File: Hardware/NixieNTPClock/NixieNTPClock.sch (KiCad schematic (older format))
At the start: 20 parts

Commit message: Add documentation with siemens datasheet Add farnel refs and component refs in schematic
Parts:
- removed Q?: BC547, Package_TO_SOT_THT:TO-92_Inline, symbol Transistor_BJT:BC547
- added Q?: BC850, Package_TO_SOT_SMD:SOT-23, symbol Transistor_BJT:BC850
- D?: value D_Shockley -> MBRS3200T3G; Farnel (none) -> 1838812
- Q?: footprint (none) -> TO_SOT_Packages_SMD:TO-252-2; Farnel (none) -> 2453852
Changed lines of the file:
@@
 EESchema Schematic File Version 4
+LIBS:NixieNTPClock-cache
 EELAYER 30 0
 EELAYER END
@@
 U 1 1 5DB6317C
 P 3750 6800
-F 0 "C?" H 3865 6846 50  0000 L CNN
+F 0 "C?" H 3800 6900 50  0000 L CNN
 F 1 "100nF" H 3800 6700 50  0000 L CNN
 F 2 "" H 3788 6650 50  0001 C CNN
@@
 	1    0    0    -1
 $EndComp
-$Comp
-L Transistor_BJT:BC547 Q?
-U 1 1 5DB638E9
-P 4200 6800
-F 0 "Q?" H 4100 6950 50  0000 L CNN
-F 1 "BC547" H 3950 6650 50  0000 L CNN
-F 2 "Package_TO_SOT_THT:TO-92_Inline" H 4400 6725 50  0001 L CIN
-F 3 "http://www.fairchildsemi.com/ds/BC/BC547.pdf" H 4200 6800 50  0001 L CNN
-	1    4200 6800
-	-1   0    0    -1
-$EndComp
 Wire Wire Line
 	3650 6450 3750 6450
-Wire Wire Line
-	4100 6450 4100 6600
 Wire Wire Line
 	3750 6450 3750 6650
@@
 Wire Wire Line
 	4100 6150 4100 6450
-Connection ~ 4100 6450
 Wire Wire Line
 	3150 5450 3150 5950
@@
 F 0 "Q?" H 4950 6350 50  0000 L CNN
 F 1 "Q_NMOS_GDS" H 5200 6300 50  0000 L CNN
-F 2 "" H 5300 6650 50  0001 C CNN
+F 2 "TO_SOT_Packages_SMD:TO-252-2" H 5300 6650 50  0001 C CNN
 F 3 "~" H 5100 6550 50  0001 C CNN
+F 4 "2453852" H 5100 6550 50  0001 C CNN "Farnel"
 	1    5100 6550
 	1    0    0    -1
@@
 P 5550 6200
 F 0 "D?" H 5550 5984 50  0000 C CNN
-F 1 "D_Shockley" H 5550 6075 50  0000 C CNN
+F 1 "MBRS3200T3G" H 5550 6075 50  0000 C CNN
 F 2 "" H 5550 6200 50  0001 C CNN
 F 3 "~" H 5550 6200 50  0001 C CNN
+F 4 "1838812" H 5550 6200 50  0001 C CNN "Farnel"
 	1    5550 6200
 	-1   0    0    1
@@
 	6500 6200 6250 6200
 Connection ~ 6250 6200
+$Comp
+L Transistor_BJT:BC850 Q?
+U 1 1 5DB5C42D
+P 4200 6800
+F 0 "Q?" H 4050 6900 50  0000 L CNN
+F 1 "BC850" H 3950 6650 50  0000 L CNN
+F 2 "Package_TO_SOT_SMD:SOT-23" H 4400 6725 50  0001 L CIN
+F 3 "http://www.infineon.com/dgdl/Infineon-BC847SERIES_BC848SERIES_BC849SERIES_BC850SERIES-DS-v01_01-en.pdf?fileId=db3a304314dca389011541d4630a1657" H 4200 6800 50  0001 L CNN
+F 4 "1081241" H 4200 6800 50  0001 C CNN "Farnel"
+	1    4200 6800
+	-1   0    0    -1
+$EndComp
+Wire Wire Line
+	4100 6600 4100 6450
+Connection ~ 4100 6450
 $EndSCHEMATC

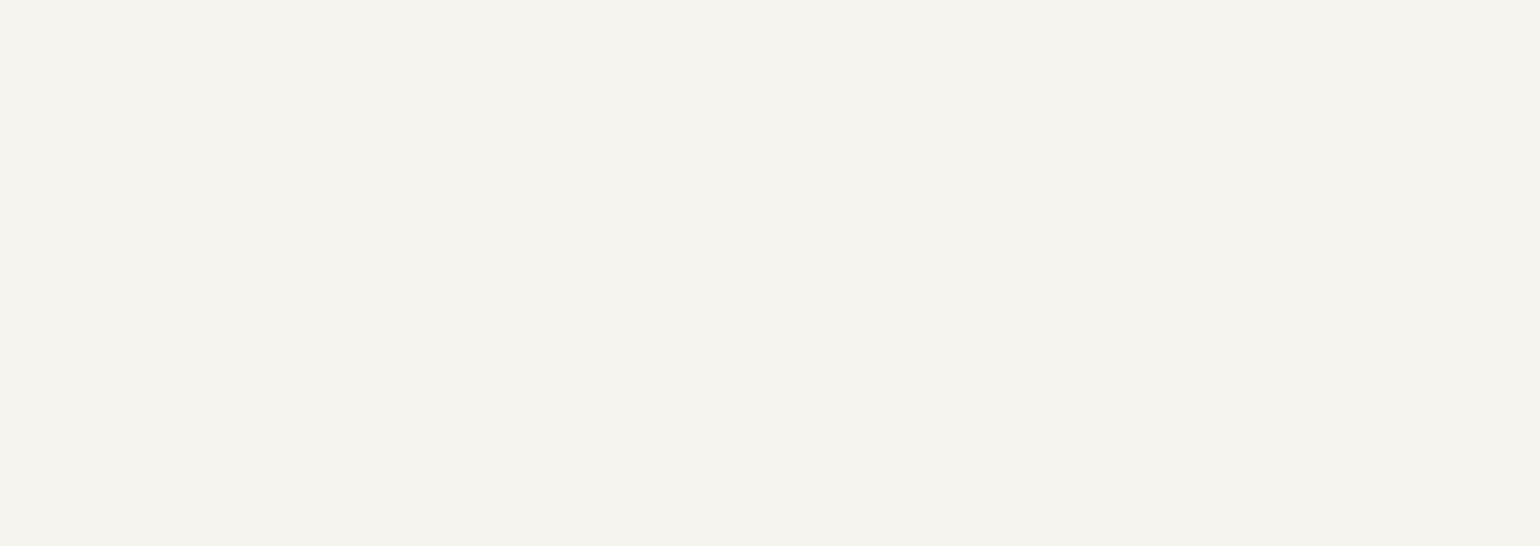
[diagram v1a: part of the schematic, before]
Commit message: Add nixie command in schema, nixie library in project and pdf in documentation
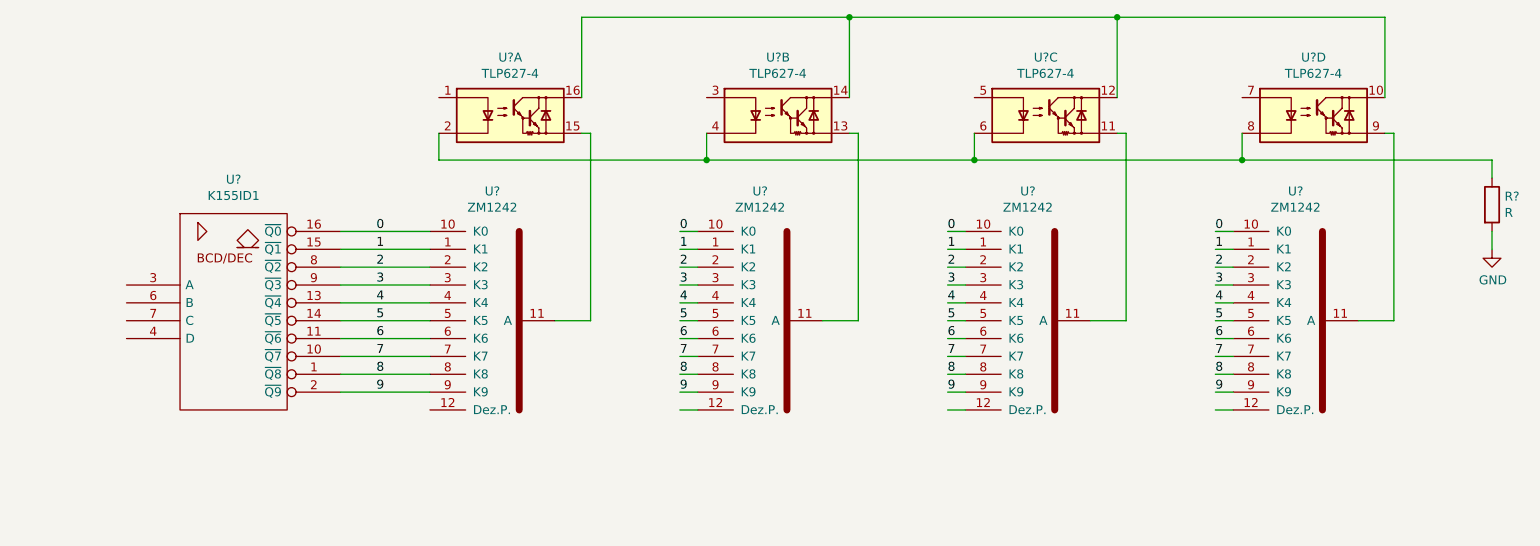
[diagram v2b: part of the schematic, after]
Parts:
- added R?: R, symbol Device:R
- added U?: K155ID1, Housings_DIP:DIP-16_W7.62mm_Socket, symbol 74xx_IEEE:74141
- added U? (x4): ZM1242, symbol nixieValve:ZM1242
- added U? (x4): TLP627-4, Package_DIP:DIP-16_W7.62mm, symbol Isolator:TLP627-4
- D?: Farnel 1838812 -> (none); Farnell (none) -> 1838812
- Q?: Farnel 1081241 -> (none); Farnell (none) -> 1081241
- Q?: Farnel 2453852 -> (none); Farnell (none) -> 2453852
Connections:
- net GND: now also R?.2, U?.12 (GND)
- new net: U?.11 (A), U?.15
- new net: U?.11 (A), U?.13
- new net: U?.11, U?.11 (A)
- new net: U?.11 (A), U?.9
- new net: U?.10, U?.12, U?.14, U?.16
- new net: R?.1, U?.2, U?.4, U?.6, U?.8
- new net 0: U?.10 (K0), U?.10 (K0), U?.10 (K0), U?.10 (K0), U?.16 (~Q0)
- new net 1: U?.1 (K1), U?.1 (K1), U?.1 (K1), U?.1 (K1), U?.15 (~Q1)
- new net 2: U?.2 (K2), U?.2 (K2), U?.2 (K2), U?.2 (K2), U?.8 (~Q2)
- new net 3: U?.3 (K3), U?.3 (K3), U?.3 (K3), U?.3 (K3), U?.9 (~Q3)
- new net 4: U?.13 (~Q4), U?.4 (K4), U?.4 (K4), U?.4 (K4), U?.4 (K4)
- new net 5: U?.14 (~Q5), U?.5 (K5), U?.5 (K5), U?.5 (K5), U?.5 (K5)
- new net 6: U?.11 (~Q6), U?.6 (K6), U?.6 (K6), U?.6 (K6), U?.6 (K6)
- new net 7: U?.10 (~Q7), U?.7 (K7), U?.7 (K7), U?.7 (K7), U?.7 (K7)
- new net 8: U?.1 (~Q8), U?.8 (K8), U?.8 (K8), U?.8 (K8), U?.8 (K8)
- new net 9: U?.2 (~Q9), U?.9 (K9), U?.9 (K9), U?.9 (K9), U?.9 (K9)
- new net VCC: U?.5 (VCC)

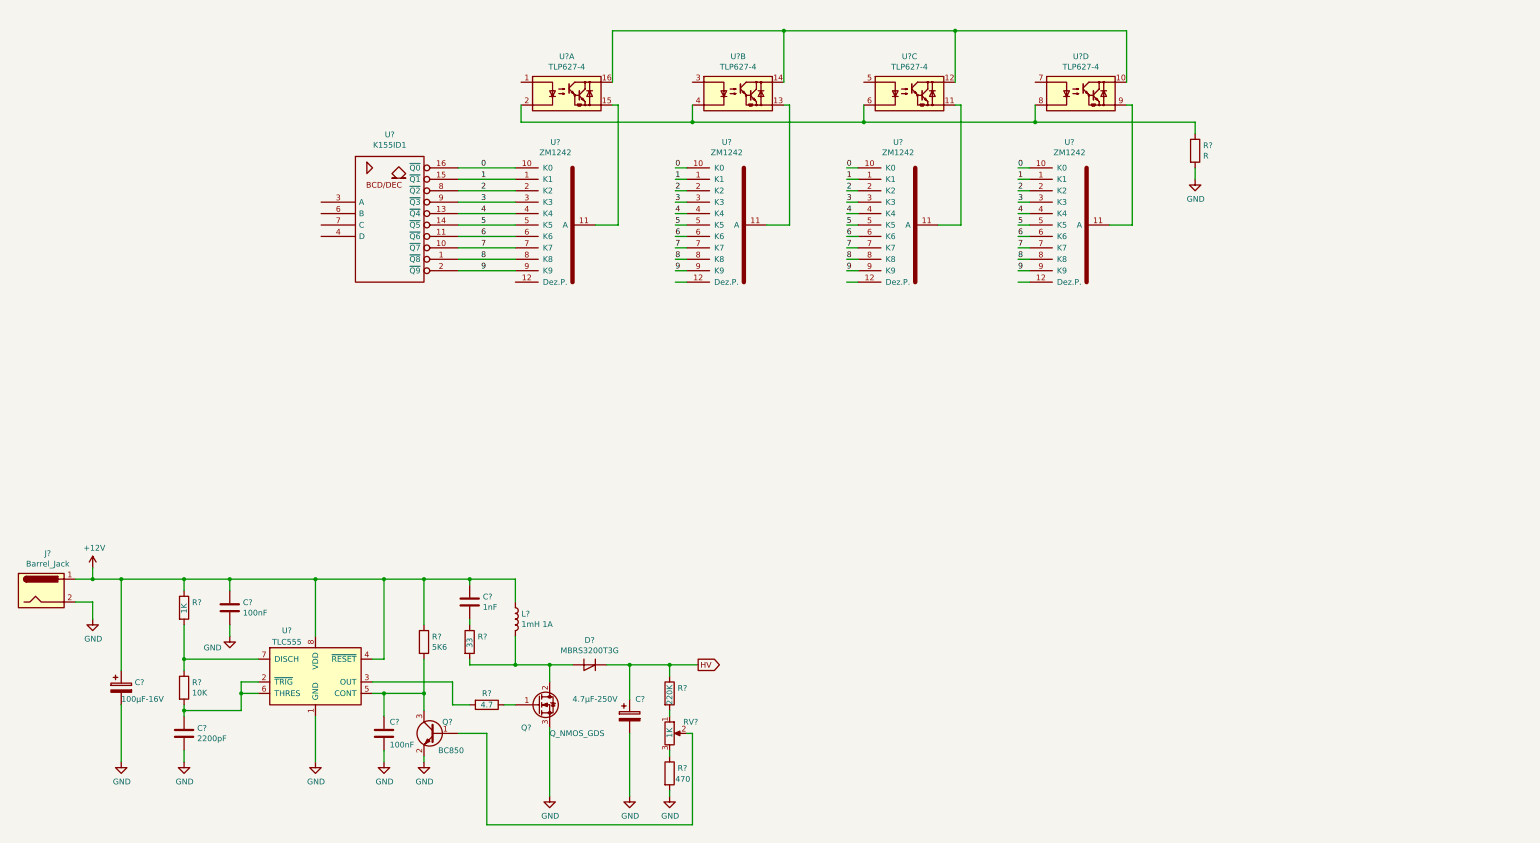
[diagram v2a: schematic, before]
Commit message: nixie command finished, add 5V DC power supply and temp sensor
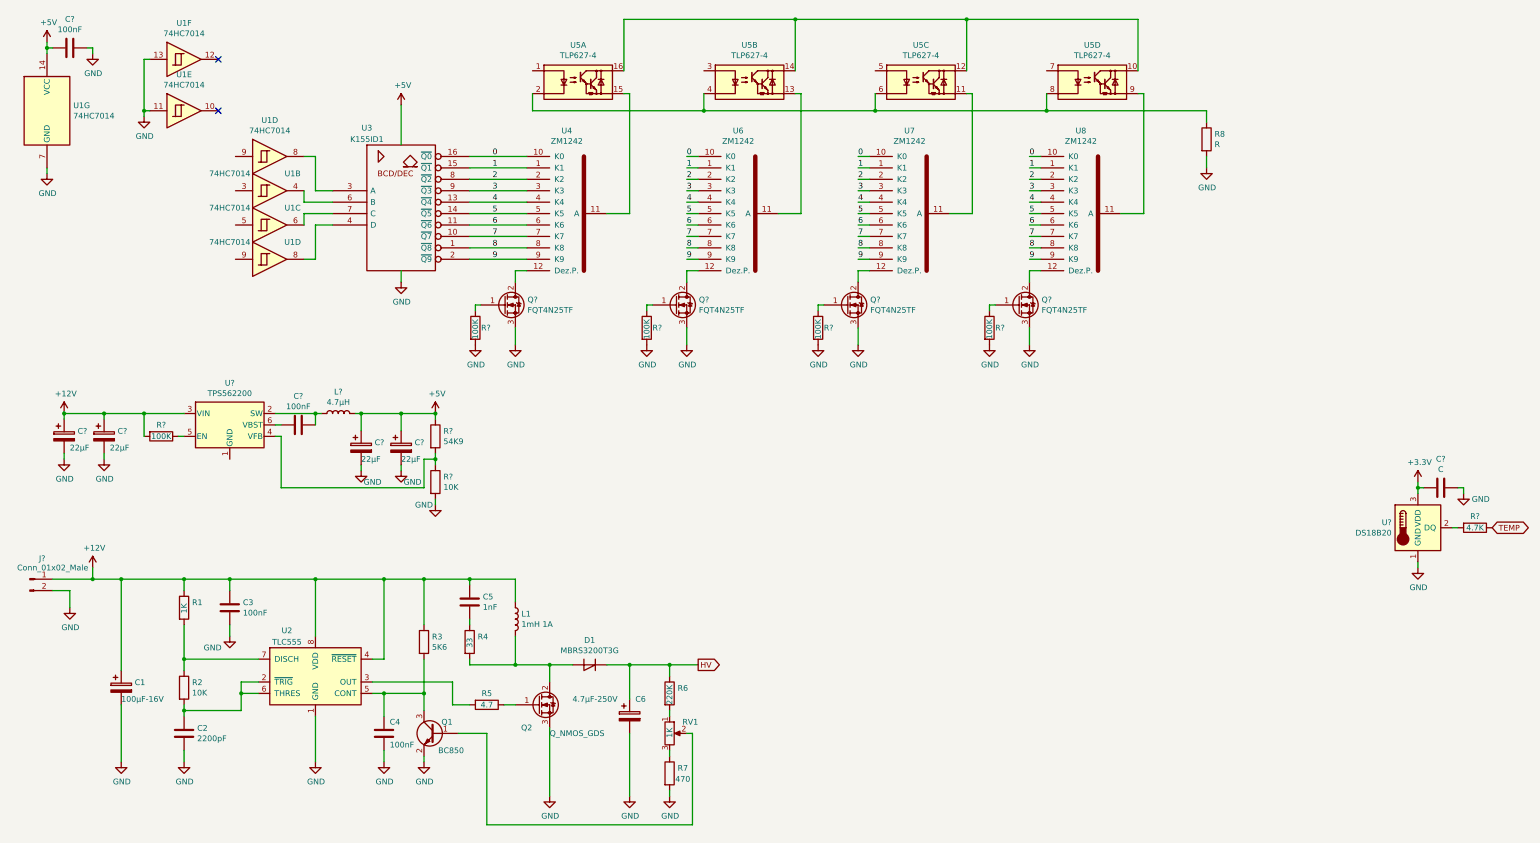
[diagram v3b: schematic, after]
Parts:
- removed J?: Barrel_Jack, symbol Connector:Barrel_Jack
- added C? (x2): 100nF, symbol Device:C
- added C?: C, symbol Device:C
- added C? (x4): 22µF, symbol Device:CP
- added J?: Conn_01x02_Male, symbol Connector:Conn_01x02_Male
- added L?: 4.7µH, symbol Device:L
- added Q? (x4): FQT4N25TF, TO_SOT_Packages_SMD:SOT-223-3_TabPin2, symbol Device:Q_NMOS_GDS
- added R?: 4.7K, symbol Device:R
- added R? (x5): 100K, symbol Device:R
- added R?: 54K9, symbol Device:R
- added R?: 10K, symbol Device:R
- added U1 (x2): 74HC7014, Package_SO:SOIC-14_3.9x8.7mm_P1.27mm, symbol 74xx:74HC7014
- added U?: DS18B20, Package_TO_SOT_THT:TO-92_Inline, symbol Sensor_Temperature:DS18B20
- added U?: TPS562200, Package_TO_SOT_SMD:SOT-23-6, symbol Regulator_Switching:TPS562200
- gave numbers to parts that had none: 26
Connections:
- net +12V: now also C?.1, C?.1, J?.1 (Pin_1), R?.2, U?.3 (VIN)
- net GND: now also C?.1, C?.1, C?.2, C?.2, C?.2, C?.2, J?.2 (Pin_2), Q?.3 (S), Q?.3 (S), Q?.3 (S), Q?.3 (S), R?.2, R?.2, R?.2, R?.2, R?.2, U1.11, U1.13, U1.7 (GND), U?.1 (GND)
- net at U3.3 (A): now also U1.8
- net at U3.4 (D): now also U1.8
- net at U3.6 (B): now also U1.4
- net at U3.7 (C): now also U1.6
- net at U4.12 (Dez.P.): now also Q?.2 (D)
- net at U6.12 (Dez.P.): now also Q?.2 (D)
- net at U7.12 (Dez.P.): now also Q?.2 (D)
- net at U8.12 (Dez.P.): now also Q?.2 (D)
- net VCC renamed +5V
- net +5V: now also C?.1, C?.1, C?.2, L?.2, R?.1, U1.14 (VCC)
- new net: R?.2, U?.2 (DQ)
- new net: Q?.1 (G), R?.1 (x4)
- new net: C?.1, L?.1, U?.2 (SW)
- new net: R?.1, R?.2, U?.4 (VFB)
- new net: R?.1, U?.5 (EN)
- new net: C?.2, U?.6 (VBST)
- new net +3V3: C?.2, U?.3 (VDD)
- new net TEMP: R?.1
- no-connect marks 0 -> 2
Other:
- moved on the sheet: R8, U3, U4, U5A, U5B, U5C, U5D, U6, U7, U8

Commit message: Add command code for farnell in schematic
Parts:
- U?: Farnell (none) -> 2781737
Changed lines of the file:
@@
 F 2 "Package_TO_SOT_SMD:SOT-23-6" H 2450 3850 50  0001 L CNN
 F 3 "http://www.ti.com/lit/ds/symlink/tps563200.pdf" H 2400 4100 50  0001 C CNN
+F 4 "2781737" H 2400 4100 50  0001 C CNN "Farnell"
 	1    2400 4100
 	1    0    0    -1

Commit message: Add ESP32 NODE MCU library + labels for connection with ESP32
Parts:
- added C?: CP, symbol Device:CP
- added C?: C, symbol Device:C
- added U?: ESP32-nodeMCU, symbol esp32:ESP32-nodeMCU
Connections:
- net +5V: now also C?.1, C?.1, U?.19 (5V)
- net GND: now also C?.2, C?.2, U?.14 (GND), U?.18 (GND), U?.32 (GND), U?.38 (GND)
- net A: now reaches U1.9
- net B: now reaches U1.3
- net C: now reaches U1.5
- net D: now reaches U1.9
- net P_UNIT_H: now reaches Q?.1 (G), R?.1
- net P_UNIT_M: now reaches Q?.1 (G), R?.1
- net DIZ_H: now reaches U5.1
- net UNIT_H: now reaches U5.3
- net DIZ_M: now reaches U5.5
- net UNIT_M: now reaches U5.7
- net P_DIZ_M: now reaches Q?.1 (G), R?.1
- net P_DIZ_H: now reaches Q?.1 (G), R?.1
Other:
- moved on the sheet: C?, R?, U?

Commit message: Add multiple references (not finished) Finish schematic
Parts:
- removed C? (x2): 100nF, symbol Device:C
- removed C? (x2): C, symbol Device:C
- removed U1: 74HC7014, Package_SO:SOIC-14_3.9x8.7mm_P1.27mm, symbol 74xx:74HC7014
- added C10, C13, C15, C8: 100nF, Capacitors_SMD:C_0805_HandSoldering, symbol Device:C
- added TP1: TestPoint, symbol Connector:TestPoint
- added unit 1 of U1
- C1: footprint (none) -> Capacitors_SMD:CP_Elec_6.3x7.7; Farnell (none) -> 1850114
- C11, C12, C7, C9: renamed from C?; footprint (none) -> Capacitors_SMD:CP_Elec_5x5.8; Farnell (none) -> 9695737
- C14: renamed from C?; value CP -> 22µF; footprint (none) -> Capacitors_SMD:CP_Elec_5x5.8; Farnell (none) -> 9695737
- C2: footprint (none) -> Capacitors_SMD:C_0603_HandSoldering; Farnell (none) -> 2470451
- C3, C4: footprint (none) -> Capacitors_SMD:C_0805_HandSoldering; Farnell (none) -> 1740665
- C5: footprint (none) -> Capacitors_SMD:C_0603_HandSoldering
- C6: footprint (none) -> Capacitors_SMD:CP_Elec_10x7.7; Farnell (none) -> 2326350
- D1: footprint (none) -> Diodes_SMD:D_SMB_Handsoldering
- J1: renamed from J?; footprint (none) -> Connect:PINHEAD1-2
- L1: footprint (none) -> Inductors:Inductor_Wurth_HCI-1335; Farnell (none) -> 2288316
- R1, R2, R3, R4, R5, R6, R7, R8: footprint (none) -> Resistors_SMD:R_1206_HandSoldering
- R10, R11, R12, R13, R14, R15, R16, R9: renamed from R?; footprint (none) -> Resistors_SMD:R_1206_HandSoldering
- RV1: footprint (none) -> Potentiometers:Potentiometer_Trimmer_Vishay_TS53YJ; Farnell (none) -> 1141482
- U2: footprint (none) -> Housings_DIP:DIP-8_W7.62mm_SMDSocket_SmallPads
- U9: renamed from U?; footprint Package_TO_SOT_SMD:SOT-23-6 -> TO_SOT_Packages_SMD:SOT-23-6
- gave numbers to parts that had none: 7
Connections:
- net +3V3: now also R14.2, U11.1 (3.3V), C13.2
- net +5V: now also C4.1, C15.1
- net A: now also U11.27 (GPIO16)
- net B: now also U1.5, U11.28 (GPIO17); no longer U1.3
- net C: now also U1.3, U11.30 (GPIO18); no longer U1.5
- net D: now also U11.31 (GPIO19), U1.1
- net DIZ_H: now also U11.7 (GPIO32)
- net DIZ_M: now also U11.9 (GPIO25)
- net GND: now also U9.1 (GND), C13.1, C15.2, C8.2
- net HV: now also U5.10, U5.12, U5.14, U5.16
- net P_DIZ_H: now also U11.11 (GPIO27)
- net P_DIZ_M: now also U11.13 (GPIO12)
- net P_UNIT_H: now also U11.12 (GPIO14)
- net P_UNIT_M: now also U11.15 (GPIO13)
- net TEMP: now also U10.2 (DQ), U11.23 (GPIO15)
- net UNIT_H: now also U11.8 (GPIO33)
- net UNIT_M: now also U11.10 (GPIO26)
- net at Q1.3 (C), R3.2, U2.5 (CONT): now also C8.1; no longer C4.1
- net at U3.4 (D): now also U1.2
- net at U3.6 (B): now also U1.6; no longer U1.4
- net at U3.7 (C): now also U1.4; no longer U1.6
- net at U11.26 (GPIO4): now also TP1.1
- net at L2.1, U9.2 (SW): now also C10.2
- net at U9.6 (VBST): now also C10.1
- no-connect marks 2 -> 18
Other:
- note added: "145V DC"
- note added: "3,3V"
- note added: "5V"
- note added: "Alimentation +145V DC"
- note added: "Alimentation +5V DC"
- moved on the sheet: R14, U1B, U1C
